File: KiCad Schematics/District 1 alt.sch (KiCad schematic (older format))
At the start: 26 parts, among them M1 Fan, P2 TERM_08

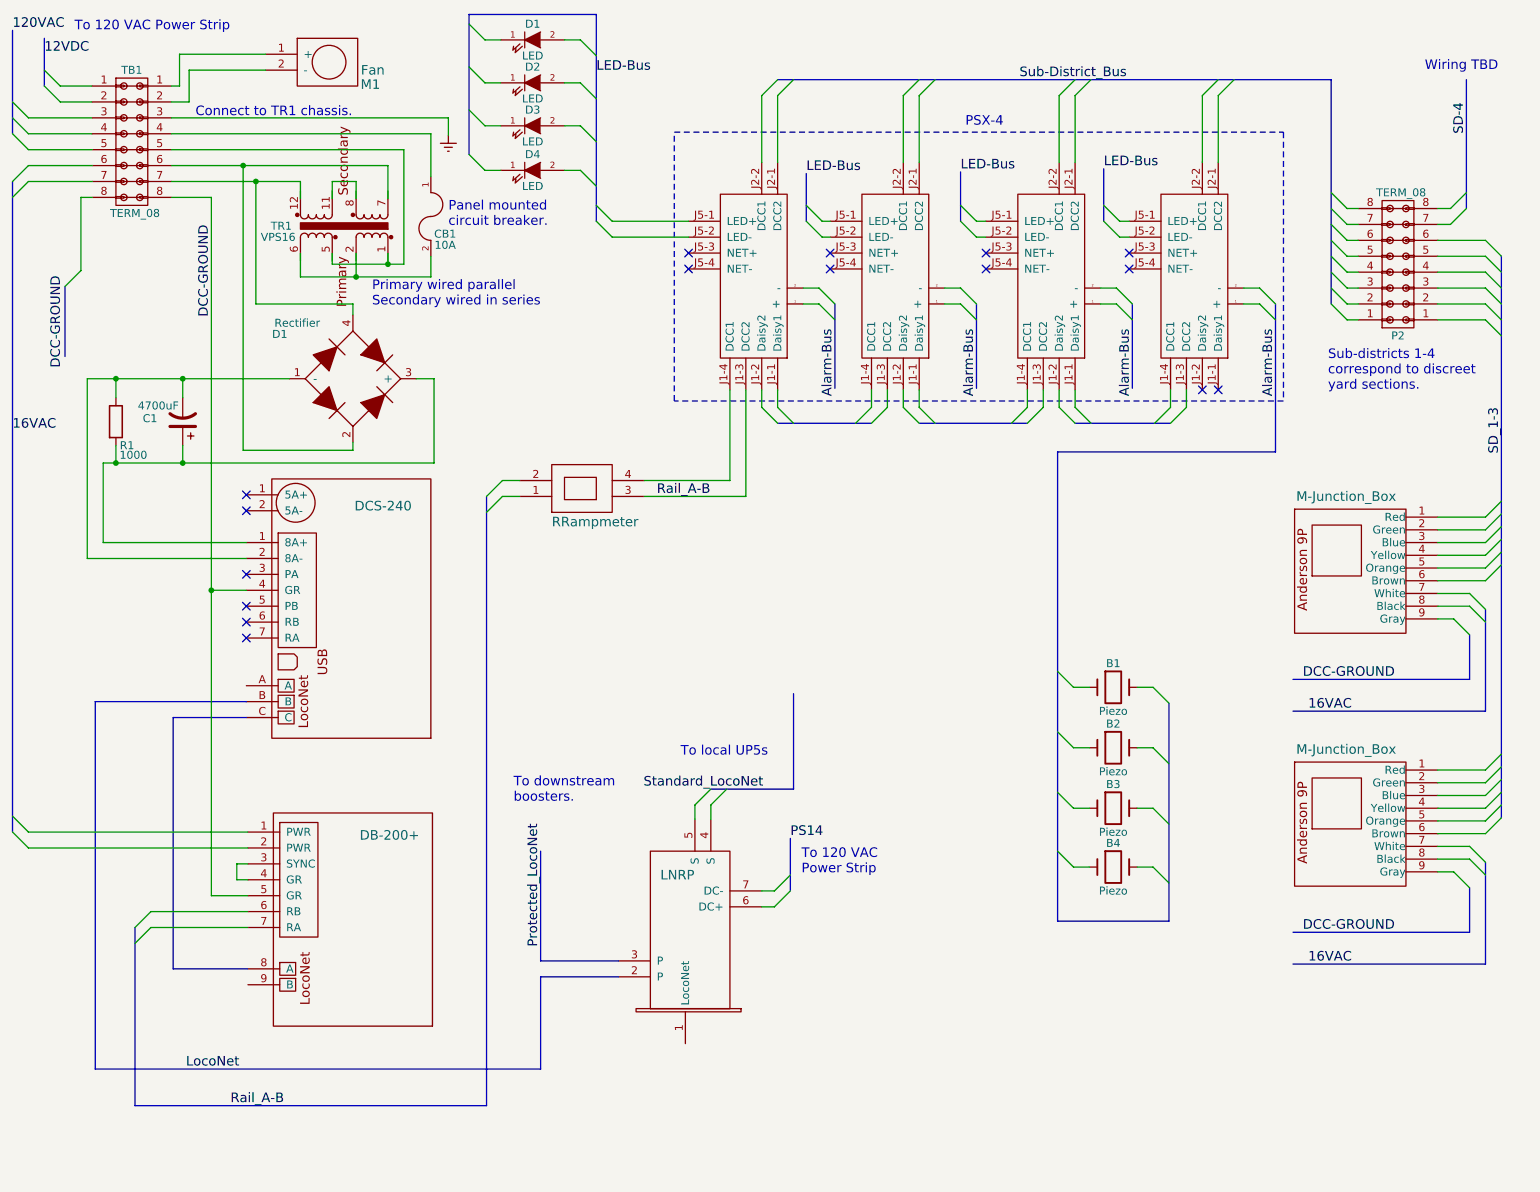
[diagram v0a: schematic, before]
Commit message: Updated schematics
Fixed wiring using the correct pin-outs for the Triad transformers. Made
other minor changes.
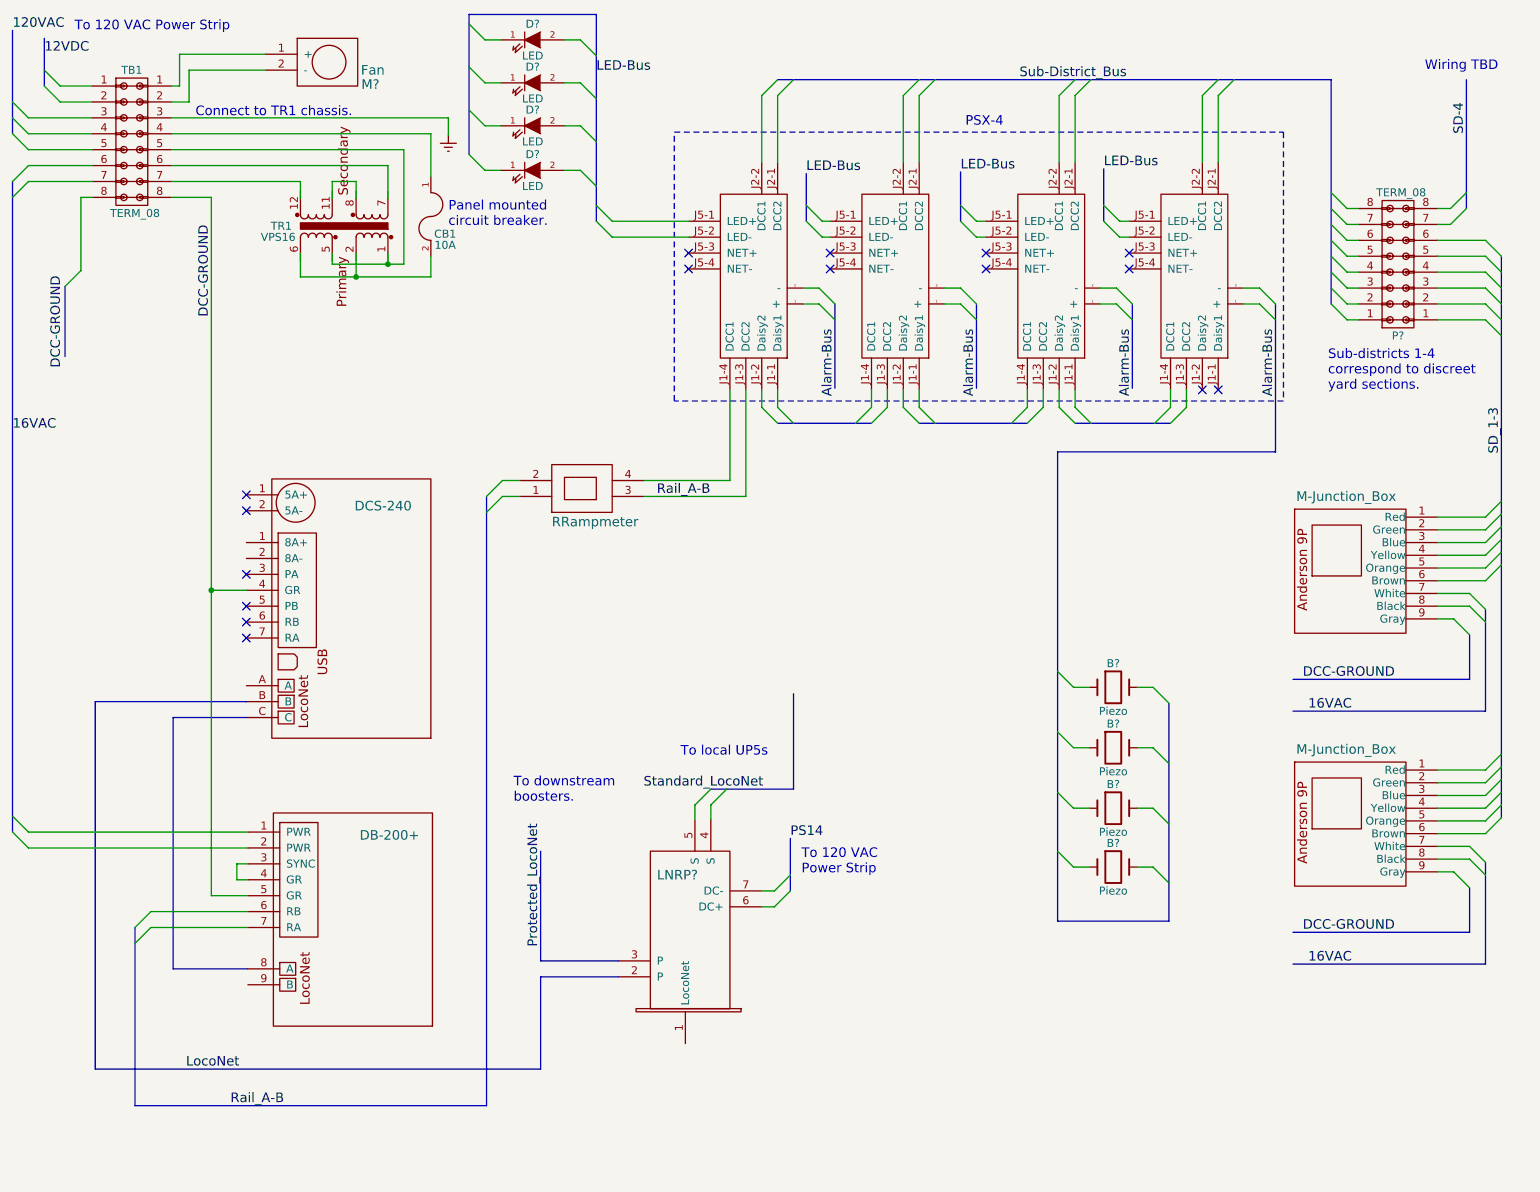
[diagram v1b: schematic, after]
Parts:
- removed B1, B2, B3, B4: Piezo, symbol Crystal
- removed C1: 4700uF, symbol CP1
- removed D1: Rectifier, symbol Diode_Bridge
- removed D1, D2, D3, D4: LED, symbol LED
- removed DB1: DB-200+, symbol DB-200+
- removed DCS1: DCS-240, symbol DCS-240
- removed LNRP: LocoNet_Repeater, symbol LocoNet_Repeater
- removed M1: Fan, symbol Fan
- removed M?: RRampmeter, symbol RRampmeter
- removed M? (x2): M-Junction_Box, symbol M-Junction_Box_No-Tap
- removed P2: TERM_08, symbol TERM_08
- removed PSX?: PSX-4, symbol PSX
- removed PSX? (x3): PSX, symbol PSX
- removed R1: 1000, symbol R
- added B? (x4): Piezo, symbol Crystal
- added D? (x4): LED, symbol LED
- added DB?: DB-200+, symbol DB-200+
- added DCS?: DCS-240, symbol DCS-240
- added LNRP?: LocoNet_Repeater, symbol LocoNet_Repeater
- added M?: Fan, symbol Fan
- added M?: RRampmeter, symbol RRampmeter
- added M? (x2): M-Junction_Box, symbol M-Junction_Box_No-Tap
- added P?: TERM_08, symbol TERM_08
- added PSX?: PSX-4, symbol PSX
- added PSX? (x3): PSX, symbol PSX
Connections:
- wire segments 160 -> 142
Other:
- note removed: "Primary wired parallel\nSecondary wired in series"
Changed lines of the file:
@@
 $Descr USLetter 11000 8500
 encoding utf-8
-Sheet 2 3
+Sheet 4 4
 Title "District 1 Power Box"
 Date "2016-08-27"
@@
 $EndDescr
 $Comp
-L LocoNet_Repeater LNRP
-U 1 1 57ACF698
+L LocoNet_Repeater LNRP?
+U 1 1 57E26DF6
 P 4560 6750
-F 0 "LNRP" V 5400 6920 60  0000 C CNN
+F 0 "LNRP?" V 5400 6920 60  0000 C CNN
 F 1 "LocoNet_Repeater" H 5000 7170 60  0001 C CNN
 F 2 "" H 4650 6980 60  0000 C CNN
@@
 $EndComp
 $Comp
-L DCS-240 DCS1
-U 1 1 57C0B903
+L DCS-240 DCS?
+U 1 1 57E26DF7
 P 2180 3420
-F 0 "DCS1" V 2440 3940 60  0001 L CNN
+F 0 "DCS?" V 2440 3940 60  0001 L CNN
 F 1 "DCS-240" V 2350 3940 60  0000 L CNN
 F 2 "" H 2170 3620 60  0000 C CNN
@@
 $EndComp
 $Comp
-L Diode_Bridge D1
-U 1 1 57C0B9F1
-P 2690 2790
-F 0 "D1" H 2230 3070 50  0000 C CNN
-F 1 "Rectifier" H 2340 3140 50  0000 C CNN
-F 2 "" H 2690 2790 50  0000 C CNN
-F 3 "" H 2690 2790 50  0000 C CNN
-	1    2690 2790
-	1    0    0    -1
-$EndComp
-$Comp
 L TERM_08 TB1
-U 1 1 57C0BA66
+U 1 1 57E26DF9
 P 1300 1300
 F 0 "TB1" H 1300 1750 50  0000 C CNN
@@
 120VAC
 $Comp
-L Fan M1
-U 1 1 57C0BEBF
+L Fan M?
+U 1 1 57E26DFA
 P 2340 650
-F 0 "M1" V 2630 1110 60  0000 C CNN
+F 0 "M?" V 2630 1110 60  0000 C CNN
 F 1 "Fan" V 2540 1050 60  0000 L CNN
 F 2 "" H 2340 650 60  0000 C CNN
@@
 $Comp
 L Earth #PWR?
-U 1 1 57C0CB4C
+U 1 1 57E26DFB
 P 3290 1260
 F 0 "#PWR?" H 3290 1010 50  0001 C CNN
@@
 	1    0    0    -1
 $EndComp
-$Comp
-L CP1 C1
-U 1 1 57C0D3F9
-P 1620 3060
-F 0 "C1" H 1780 3040 50  0000 L CNN
-F 1 "4700uF" H 1645 2960 50  0000 L CNN
-F 2 "" H 1620 3060 50  0000 C CNN
-F 3 "" H 1620 3060 50  0000 C CNN
-	1    1620 3060
-	-1   0    0    1
-$EndComp
 Entry Wire Line
 	550  1550 650  1450
@@
 $Comp
 L PSX PSX?
-U 1 1 57C0F322
+U 1 1 57E26DFD
 P 5420 2660
 F 0 "PSX?" H 5450 3140 60  0001 L CNN
@@
 $Comp
 L PSX PSX?
-U 1 1 57C0F49B
+U 1 1 57E26DFE
 P 6310 2660
 F 0 "PSX?" H 6340 3140 60  0001 L CNN
@@
 $Comp
 L PSX PSX?
-U 1 1 57C0F55C
+U 1 1 57E26DFF
 P 7290 2660
 F 0 "PSX?" H 7320 3140 60  0001 L CNN
@@
 NoConn ~ 2020 4420
 $Comp
-L DB-200+ DB1
-U 1 1 57C10EE5
+L DB-200+ DB?
+U 1 1 57E26E00
 P 2190 5520
-F 0 "DB1" H 2310 6350 60  0001 C CNN
+F 0 "DB?" H 2310 6350 60  0001 C CNN
 F 1 "DB-200+" V 2330 6250 60  0000 C CNN
 F 2 "" H 2180 5720 60  0000 C CNN
@@
 $Comp
 L PSX PSX?
-U 1 1 57C1340D
+U 1 1 57E26E01
 P 8190 2660
 F 0 "PSX?" H 8220 3140 60  0001 L CNN
@@
 	7230 2970 7330 3070
 $Comp
-L LED D3
-U 1 1 57C158DE
+L LED D?
+U 1 1 57E26E02
 P 3820 1200
-F 0 "D3" H 3820 1300 50  0000 C CNN
+F 0 "D?" H 3820 1300 50  0000 C CNN
 F 1 "LED" H 3820 1100 50  0000 C CNN
 F 2 "" H 3820 1200 50  0000 C CNN
@@
 $EndComp
 $Comp
-L LED D2
-U 1 1 57C15C6C
+L LED D?
+U 1 1 57E26E03
 P 3820 930
-F 0 "D2" H 3820 1030 50  0000 C CNN
+F 0 "D?" H 3820 1030 50  0000 C CNN
 F 1 "LED" H 3820 830 50  0000 C CNN
 F 2 "" H 3820 930 50  0000 C CNN
@@
 $EndComp
 $Comp
-L LED D4
-U 1 1 57C15FA5
+L LED D?
+U 1 1 57E26E04
 P 3820 1480
-F 0 "D4" H 3820 1580 50  0000 C CNN
+F 0 "D?" H 3820 1580 50  0000 C CNN
 F 1 "LED" H 3820 1380 50  0000 C CNN
 F 2 "" H 3820 1480 50  0000 C CNN
@@
 $EndComp
 $Comp
-L LED D1
-U 1 1 57C16002
+L LED D?
+U 1 1 57E26E05
 P 3820 660
-F 0 "D1" H 3820 760 50  0000 C CNN
+F 0 "D?" H 3820 760 50  0000 C CNN
 F 1 "LED" H 3820 560 50  0000 C CNN
 F 2 "" H 3820 660 50  0000 C CNN
@@
 $Comp
 L RRampmeter M?
-U 1 1 57C211A4
+U 1 1 57E26E06
 P 3940 3630
 F 0 "M?" V 3800 3690 60  0001 C CNN
@@
 Standard_LocoNet
 $Comp
-L TERM_08 P2
-U 1 1 57C2519F
+L TERM_08 P?
+U 1 1 57E26E07
 P 9260 2070
-F 0 "P2" H 9260 2520 50  0000 C CNN
+F 0 "P?" H 9260 2520 50  0000 C CNN
 F 1 "TERM_08" H 9280 1620 50  0000 C CNN
 F 2 "" H 9260 870 50  0000 C CNN
@@
 $Comp
 L M-Junction_Box_No-Tap M?
-U 1 1 57C28D22
+U 1 1 57E26E08
 P 8610 3610
 F 0 "M?" H 8680 3450 60  0001 C CNN
@@
 Wire Wire Line
 	1550 1450 2910 1450
-Connection ~ 2080 1550
-Wire Wire Line
-	2000 1450 2000 3240
-Connection ~ 2000 1450
-Wire Wire Line
-	1020 2790 2290 2790
-Wire Wire Line
-	1020 2790 1020 3920
-Wire Wire Line
-	1020 3920 2020 3920
-Wire Wire Line
-	1120 3320 1120 3820
-Wire Wire Line
-	1120 3820 2020 3820
 Wire Wire Line
 	1050 1450 650  1450
 Wire Wire Line
 	1050 1550 650  1550
-Wire Wire Line
-	1550 1650 1800 1650
-Wire Wire Line
-	1800 1650 1800 6040
 Wire Wire Line
 	1800 4120 2020 4120
@@
 	1660 850  2140 850
 Wire Wire Line
-	2690 3190 2690 3240
-Wire Wire Line
-	2690 3240 2000 3240
-Wire Wire Line
-	2690 2390 2690 2320
-Wire Wire Line
-	2690 2320 2080 2320
-Wire Wire Line
-	2080 2320 2080 1550
-Wire Wire Line
-	1120 3320 3200 3320
-Wire Wire Line
-	3200 3320 3200 2790
-Wire Wire Line
-	3200 2790 3090 2790
-Wire Wire Line
-	1620 2910 1620 2790
-Connection ~ 1620 2790
-Wire Wire Line
-	1620 3210 1620 3320
-Connection ~ 1620 3320
-Wire Wire Line
 	3620 660  3520 660
 Wire Wire Line
@@
 Wire Bus Line
 	4220 500  4220 1800
-Text Notes 2810 2340 0    60   ~ 0
-Primary wired parallel\nSecondary wired in series
 Text Notes 5510 5910 0    60   ~ 0
 To 120 VAC\nPower Strip
@@
 	5060 2860 5060 3430
 $Comp
-L Crystal B2
-U 1 1 57C2E519
+L Crystal B?
+U 1 1 57E26E09
 P 7470 5110
-F 0 "B2" H 7470 5260 50  0000 C CNN
+F 0 "B?" H 7470 5260 50  0000 C CNN
 F 1 "Piezo" H 7470 4960 50  0000 C CNN
 F 2 "" H 7470 5110 50  0000 C CNN
@@
 $EndComp
 $Comp
-L Crystal B3
-U 1 1 57C2E622
+L Crystal B?
+U 1 1 57E26E0A
 P 7470 5490
-F 0 "B3" H 7470 5640 50  0000 C CNN
+F 0 "B?" H 7470 5640 50  0000 C CNN
 F 1 "Piezo" H 7470 5340 50  0000 C CNN
 F 2 "" H 7470 5490 50  0000 C CNN
@@
 $EndComp
 $Comp
-L Crystal B4
-U 1 1 57C2E6BB
+L Crystal B?
+U 1 1 57E26E0B
 P 7470 5860
-F 0 "B4" H 7470 6010 50  0000 C CNN
+F 0 "B?" H 7470 6010 50  0000 C CNN
 F 1 "Piezo" H 7470 5710 50  0000 C CNN
 F 2 "" H 7470 5860 50  0000 C CNN
@@
 $EndComp
 $Comp
-L Crystal B1
-U 1 1 57C2E788
+L Crystal B?
+U 1 1 57E26E0C
 P 7470 4730
-F 0 "B1" H 7470 4880 50  0000 C CNN
+F 0 "B?" H 7470 4880 50  0000 C CNN
 F 1 "Piezo" H 7470 4580 50  0000 C CNN
 F 2 "" H 7470 4730 50  0000 C CNN
@@
 Text Notes 9890 860  2    60   ~ 0
 Wiring TBD
-$Comp
-L R R1
-U 1 1 57C2E4CC
-P 1200 3060
-F 0 "R1" H 1270 2910 50  0000 C CNN
-F 1 "1000" H 1310 2850 50  0000 C CNN
-F 2 "" V 1130 3060 50  0000 C CNN
-F 3 "" H 1200 3060 50  0000 C CNN
-	1    1200 3060
-	1    0    0    -1
-$EndComp
-Wire Wire Line
-	1200 2910 1200 2790
-Connection ~ 1200 2790
-Wire Wire Line
-	1200 3210 1200 3320
-Connection ~ 1200 3320
 Wire Bus Line
 	3870 7130 1070 7130
@@
 $Comp
 L FUSE CB1
-U 1 1 57C49525
+U 1 1 57E26E0E
 P 3180 1770
 F 0 "CB1" V 3290 1860 50  0000 C CNN
@@
 $Comp
 L M-Junction_Box_No-Tap M?
-U 1 1 57C4EDF8
+U 1 1 57E26E0F
 P 8610 5200
 F 0 "M?" H 8680 5040 60  0001 C CNN
@@
 $Comp
 L TRANSFORMER_VPS16 TR1
-U 1 1 57E17910
+U 1 1 57E26E10
 P 2620 1830
 F 0 "TR1" V 2620 2210 50  0000 C CNN
@@
 Wire Wire Line
 	2710 1550 2710 1660
+Wire Wire Line
+	1550 1650 1800 1650
+Wire Wire Line
+	1800 1650 1800 6040
 $EndSCHEMATC
